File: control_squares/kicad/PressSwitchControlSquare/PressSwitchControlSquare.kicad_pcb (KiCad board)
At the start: 2 copper layers, 63.5 x 31.8 mm, 6 parts

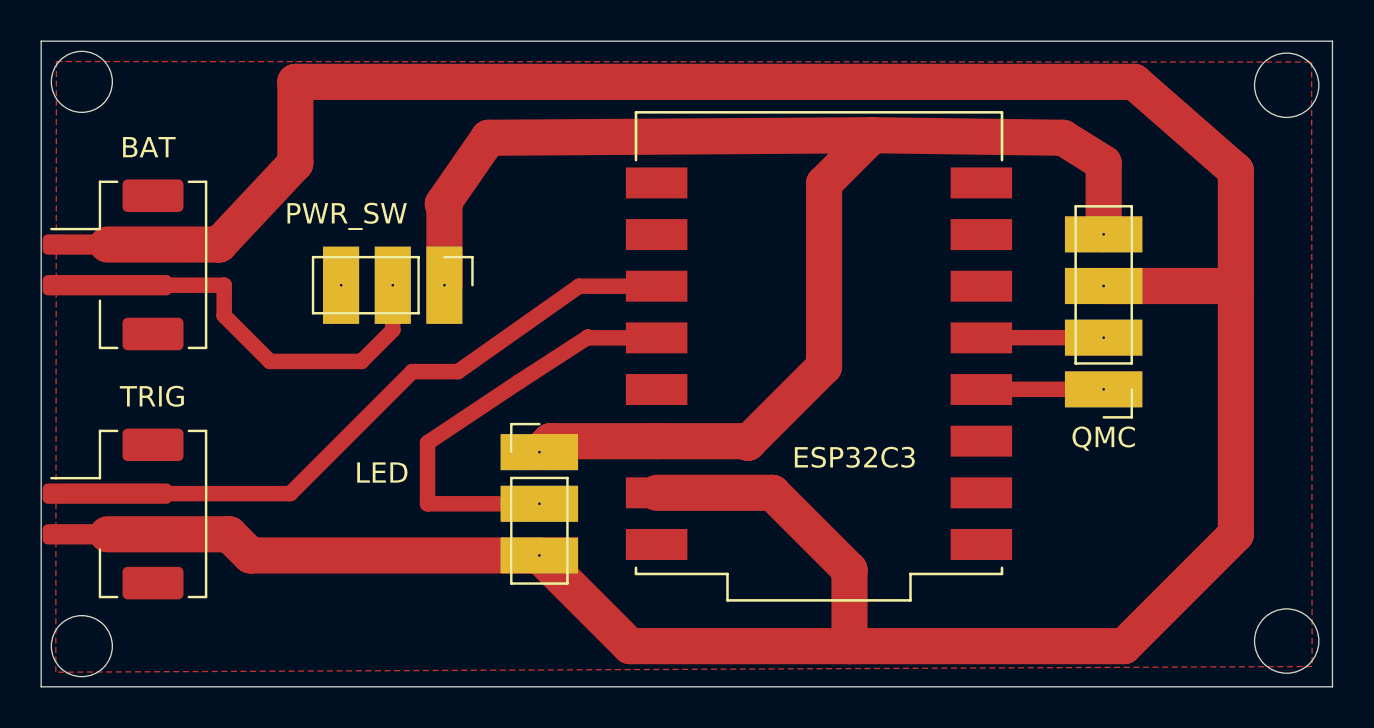
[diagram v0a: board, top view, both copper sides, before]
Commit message: added another pin to trigger
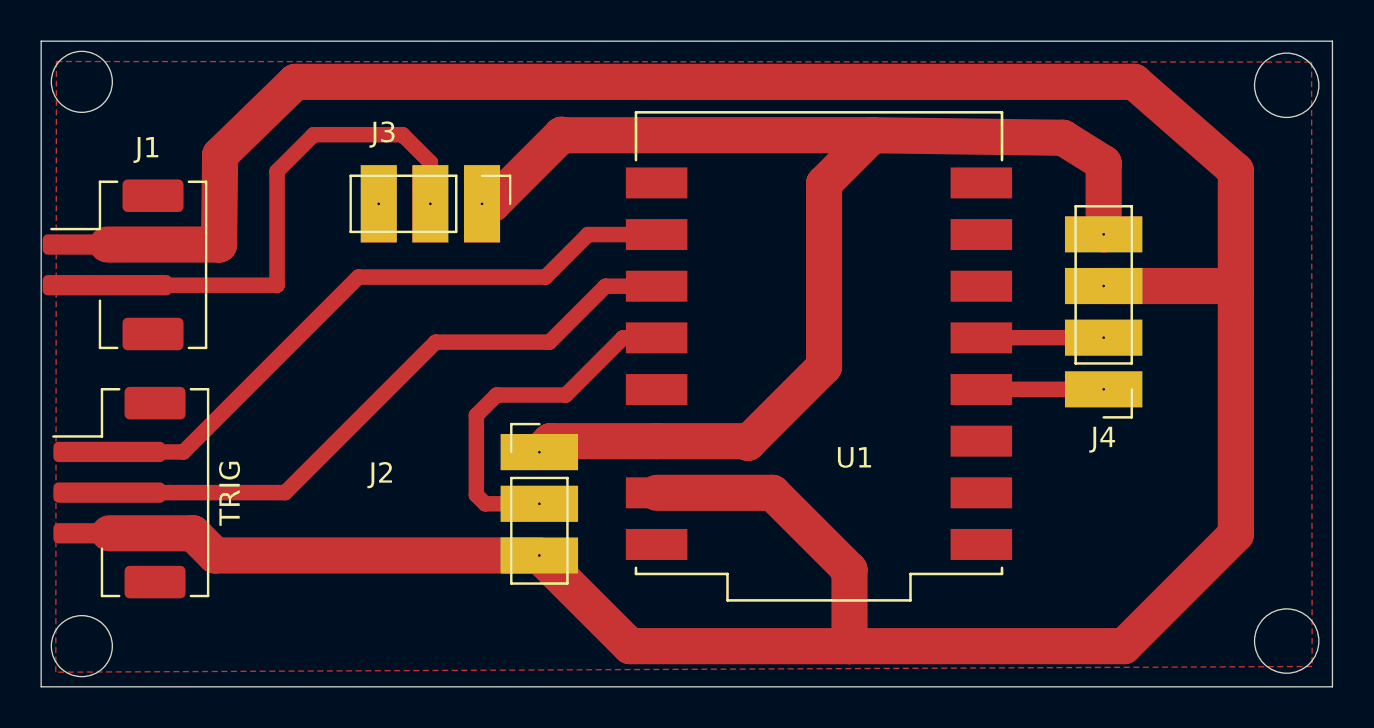
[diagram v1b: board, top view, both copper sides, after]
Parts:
- removed the TRIG at (3.75, 23.2)
- added TRIG: TRIG, Connector_JST:JST_PH_B3B-PH-SM4-TB_1x03-1MP_P2.00mm_Vertical, F.Cu at (3.85, 22.2)
- J1: renamed from BAT; value BAT -> Battery
- J3: renamed from PWR_SW; value PWR_SW -> Batt_switch
- moved J3 4.41 mm to (21.7, 8.00)
- renumbered LED to J2, QMC to J4, ESP32C3 to U1
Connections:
- U1 pad 1: unconnected-(U1-GPIO1-Pad1) -> Net-(J5-Pin_1)
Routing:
- net Net-(J5-Pin_1): track 0.00 -> 31.3 mm
- net +3V3: track 70.3 -> 64.0 mm
- net Net-(J1-Pin_2): track 19.3 -> 24.8 mm
- net SIG: track 21.5 -> 17.6 mm

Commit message: added voltage regulator
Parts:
- added C1: C, Capacitor_SMD:C_0603_1608Metric, F.Cu at (10.2, 6.60)
- added C2: C, Capacitor_SMD:C_0603_1608Metric, F.Cu at (10.2, 3.20)
- added U2: AP2112K-3.3TRG1, AP2112K-3.3TRG1:SOT95P285X140-5N, F.Cu at (12.2, 10.0)
- added VSEL1: VSelect, Connector_PinHeader_2.54mm:PinHeader_1x03_P2.54mm_Vertical, F.Cu at (18.5, 4.60)
- J5: renamed from TRIG; value TRIG -> Conn_01x03_Pin
- moved J3 2.45 mm to (23.3, 9.80)
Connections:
- J3 pad 1: +3V3 -> Net-(J3-Pin_1)
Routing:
- net GND: track 162.2 -> 120.6 mm
- net Net-(U2-EN): track 0.00 -> 25.4 mm
- net +3V3: track 64.0 -> 82.0 mm, vias 0 -> 2
- net Net-(J3-Pin_1): track 0.00 -> 6.17 mm
- net Net-(J5-Pin_1): track 31.3 -> 34.4 mm
- net Net-(J1-Pin_2): track 24.8 -> 21.9 mm
- net Net-(J5-Pin_2): track 31.1 -> 33.5 mm

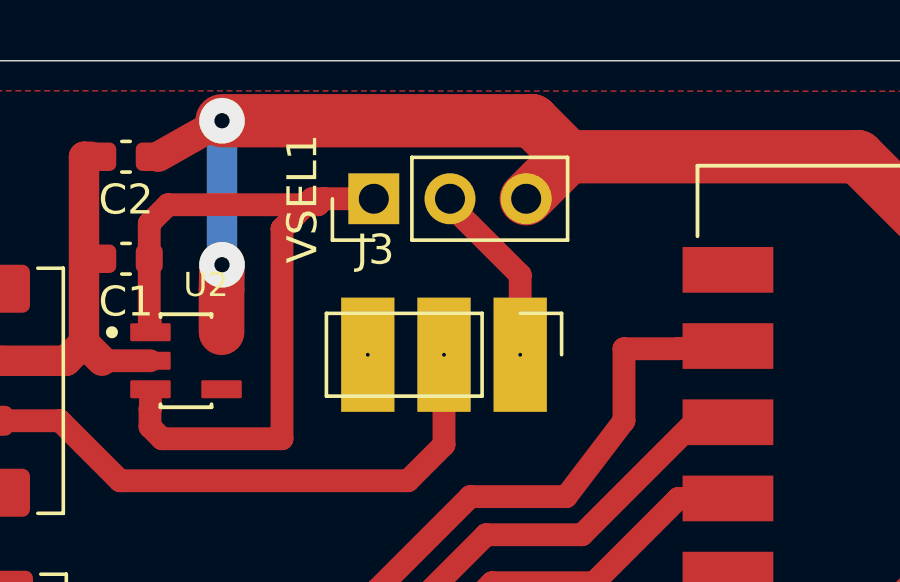
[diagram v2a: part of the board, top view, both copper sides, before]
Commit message: added another pin to trigger
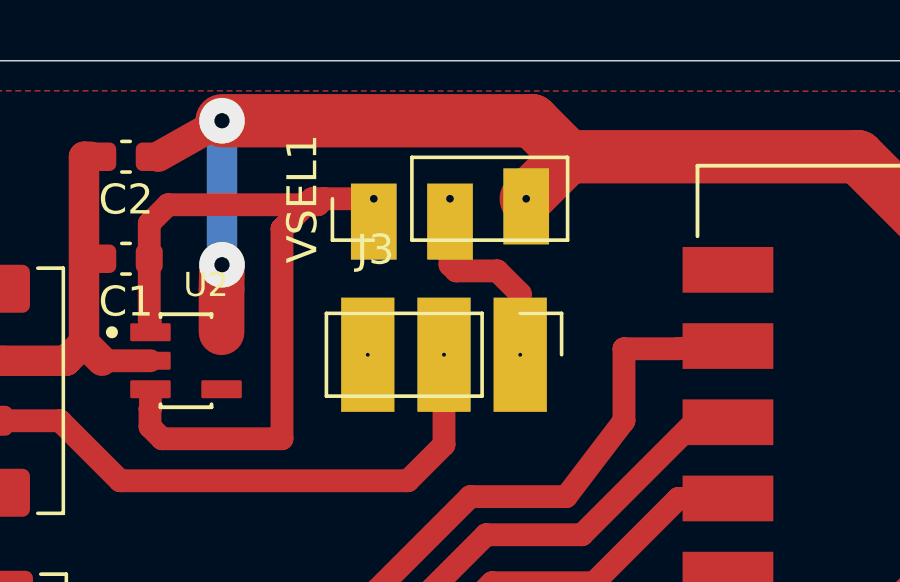
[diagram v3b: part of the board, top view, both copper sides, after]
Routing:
- net Net-(J3-Pin_1): track 6.17 -> 6.97 mm
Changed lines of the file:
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@@
 		(pad "1" thru_hole rect
 			(at 0 0 90)
-			(size 1.7 1.7)
-			(drill 1)
+			(size 2.54 1.524)
+			(drill 0.254
+				(offset -0.762 0)
+			)
 			(layers "*.Cu" "*.Mask")
 			(remove_unused_layers no)
@@
 			(pintype "passive")
 		)
-		(pad "2" thru_hole circle
+		(pad "2" thru_hole rect
 			(at 0 2.54 90)
-			(size 1.7 1.7)
-			(drill 1)
+			(size 2.54 1.524)
+			(drill 0.254
+				(offset -0.762 0)
+			)
 			(layers "*.Cu" "*.Mask")
 			(remove_unused_layers no)
@@
 			(pintype "passive")
 		)
-		(pad "3" thru_hole circle
+		(pad "3" thru_hole rect
 			(at 0 5.08 90)
-			(size 1.7 1.7)
-			(drill 1)
+			(size 2.54 1.524)
+			(drill 0.254
+				(offset -0.254 0)
+			)
 			(layers "*.Cu" "*.Mask")
 			(remove_unused_layers no)
@@
 	)
 	(segment
-		(start 23.34 7.14)
+		(start 23.34 7.766)
 		(end 23.34 9.8)
 		(width 0.762)
@@
 	(segment
 		(start 21 4.6)
-		(end 21 4.8)
+		(end 21 6.8)
 		(width 0.762)
 		(layer "F.Cu")
@@
 	)
 	(segment
-		(start 21 4.8)
-		(end 23.34 7.14)
-		(width 0.762)
-		(layer "F.Cu")
+		(start 22.579 7.005)
+		(end 23.34 7.766)
+		(width 0.762)
+		(layer "F.Cu")
+		(net 19)
+	)
+	(segment
+		(start 21 6.8)
+		(end 21.205 7.005)
+		(width 0.762)
+		(layer "F.Cu")
+		(net 19)
+	)
+	(segment
+		(start 21.205 7.005)
+		(end 22.579 7.005)
+		(width 0.762)
+		(layer "F.Cu")

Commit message: fixed issues with board
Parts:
- moved J3 10.7 mm to (16.3, 17.8)
- moved VSEL1 7.05 mm to (22.9, 10.1), turned to 180 degrees
- moved U2 3.61 mm to (15.6, 11.2)
- moved U1 3.26 mm to (38.0, 18.1)
- moved J2 3.07 mm to (23.8, 23.2)
- moved C2 2.06 mm to (10.7, 5.20)
- moved C1 1.58 mm to (10.7, 8.10)
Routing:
- net GND: track 120.6 -> 175.0 mm
- net Net-(J3-Pin_1): track 6.97 -> 20.5 mm
- net Net-(J1-Pin_2): track 21.9 -> 14.3 mm
- net Net-(J5-Pin_2): track 33.5 -> 29.5 mm
- net Net-(J5-Pin_1): track 34.4 -> 30.9 mm
- net SCL: track 6.12 -> 9.15 mm
- net SDA: track 6.12 -> 8.69 mm
- net Net-(U2-EN): track 25.4 -> 27.2 mm
- net SIG: track 17.6 -> 18.4 mm
